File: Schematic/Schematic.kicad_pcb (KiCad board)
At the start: 2 copper layers, 29.6 x 24.1 mm, 12 parts, among them J1 Conn_01x04_Pin, U1 STM32F401CCUx

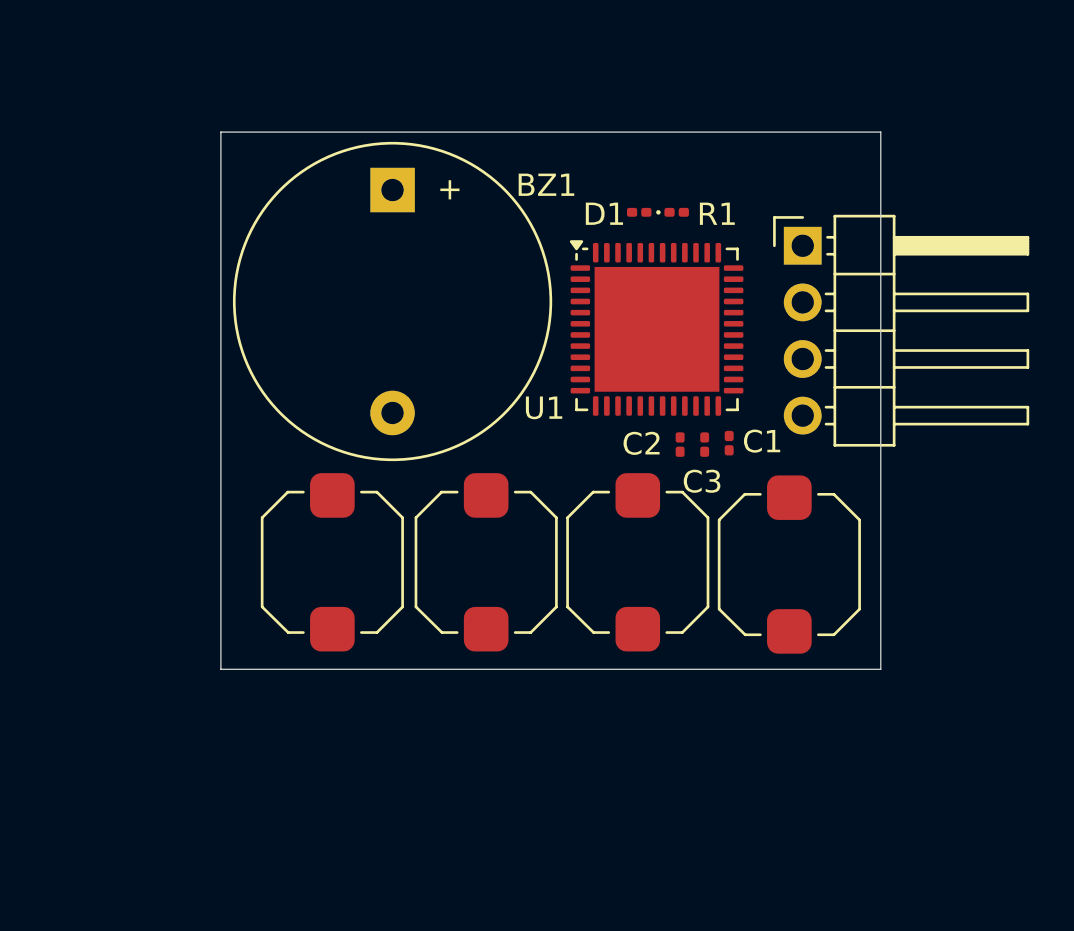
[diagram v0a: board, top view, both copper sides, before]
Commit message: Debugging totalSprintTime_
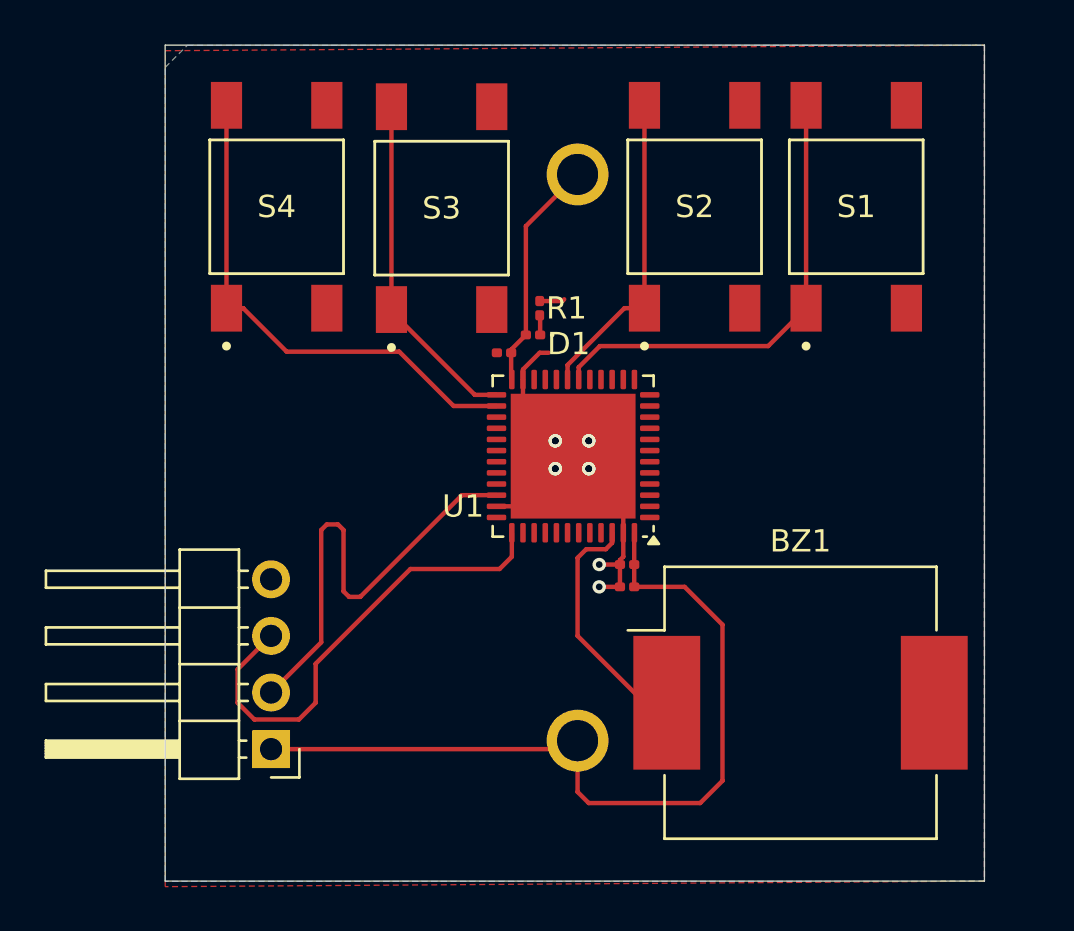
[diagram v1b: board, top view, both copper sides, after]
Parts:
- removed DOWN1, PLAY_PAUSE1, TOGGLE1, UP1: SW_Push, Button_Switch_SMD:SW_Push_1TS009xxxx-xxxx-xxxx_6x6x5mm
- added BT1: 3007, 3007:BAT_3007, B.Cu at (134.0, 90.0)
- added S1: PLAY_PAUSE, TS04_66_73_BK_100_SMT:SW_TS04-66-73-BK-100-SMT, F.Cu at (146.5, 78.8)
- added S2: TOGGLE, TS04_66_73_BK_100_SMT:SW_TS04-66-73-BK-100-SMT, F.Cu at (139.2, 78.8)
- added S3: UP, TS04_66_73_BK_100_SMT:SW_TS04-66-73-BK-100-SMT, F.Cu at (127.9, 78.8)
- added S4: DOWN, TS04_66_73_BK_100_SMT:SW_TS04-66-73-BK-100-SMT, F.Cu at (120.5, 78.8)
- BZ1: footprint Buzzer_Beeper:Buzzer_D14mm_H7mm_P10mm -> Buzzer_Beeper:Buzzer_Mallory_AST1240MLQ
- moved J1 32.8 mm to (120.2, 103.1), turned to 180 degrees
- moved BZ1 29.4 mm to (144.0, 101.0), turned to 0 degrees
- moved C2 8.91 mm to (130.7, 85.3), turned to 180 degrees
- moved R1 7.50 mm to (132.3, 83.3), turned to 90 degrees
- moved D1 7.28 mm to (132.0, 84.5)
- moved C3 7.27 mm to (136.2, 95.8), turned to 180 degrees
- moved C1 7.12 mm to (136.2, 94.8), turned to 180 degrees
- moved U1 6.82 mm to (133.8, 89.9), turned to 180 degrees
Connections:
- U1 pad 36: unconnected-(U1-VDD-Pad36) -> 3V3
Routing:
- net 3V3: track 0.00 -> 47.9 mm
- net Down: track 0.00 -> 23.0 mm
- net SWCLK: track 0.00 -> 21.4 mm
- net SWDIO: track 0.00 -> 21.0 mm
- net Play: track 0.00 -> 20.9 mm
- net GND: track 0.00 -> 20.5 mm, vias 0 -> 10
- net Up: track 0.00 -> 15.4 mm
- net Tog: track 0.00 -> 14.3 mm
- net Buz: track 0.00 -> 10.0 mm
- net Net-(D1-K): track 0.00 -> 0.89 mm
- added copper zone on B.Cu, net GND
- added copper zone on F.Cu, net GND
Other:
- board size 29.6 x 24.1 mm -> 36.8 x 37.5 mm

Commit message: Schematic stuff
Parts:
- added C4: 100nF, Capacitor_SMD:C_0201_0603Metric, F.Cu at (136.2, 96.2)
- added C5: 100nF, Capacitor_SMD:C_0201_0603Metric, F.Cu at (136.2, 97.1)
- added C6: 100nF, Capacitor_SMD:C_0201_0603Metric, F.Cu at (139.0, 92.8)
- added C7: 4.7uF, Capacitor_SMD:C_0201_0603Metric, F.Cu at (139.0, 93.7)
- added C8: 4.7uF, Capacitor_SMD:C_0201_0603Metric, F.Cu at (132.4, 85.4)
- moved C3 0.40 mm to (136.2, 95.4)
- moved C1 0.20 mm to (136.2, 94.6)
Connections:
- BT1 pad P2: 3V3 -> (no net)
- U1 pad 22: unconnected-(U1-VCAP1-Pad22) -> Net-(U1-VCAP1)
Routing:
- net 3V3: track 47.9 -> 55.0 mm
- net GND: track 20.5 -> 18.3 mm, vias 10 -> 11
- net Net-(U1-VCAP1): track 0.00 -> 1.11 mm
